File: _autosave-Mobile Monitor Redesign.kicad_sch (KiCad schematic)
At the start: 48 parts, among them J1 Conn_01x02_Pin, J2 Conn_01x08_Pin, J3 Conn_01x08_Pin, J5 Conn_02x03_Odd_Even, J6 Micro_SD_Card_Det1, J7 Conn_01x05_Pin, J8 Conn_01x06_Socket, Q1 2N7002, Q2 AO3401A, Q3 BSS138, Q4 BSS138, U1 ATmega2560-16A, U11 TPL5010, U2 DS3232M, U3 AP2112K-3.3, U4 L80-R, U7 CH340C, Y2 Crystal

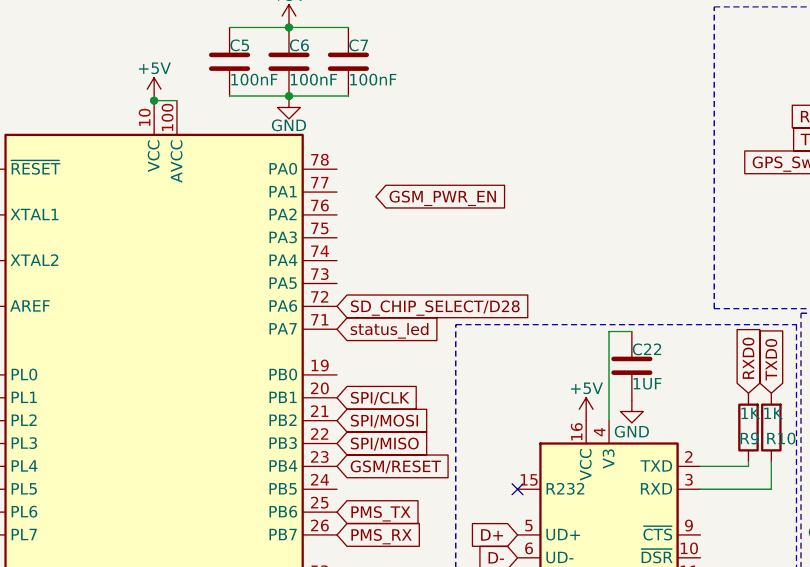
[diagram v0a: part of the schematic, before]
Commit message: added 3.3v logic level  shifting for battery monitoring chip I2C lines
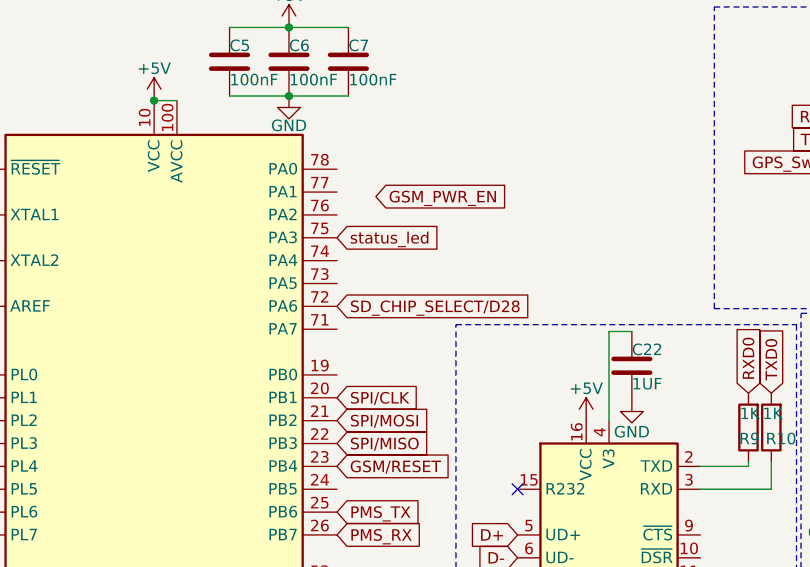
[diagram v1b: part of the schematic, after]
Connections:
- net status_led: now also U1.75 (PA3); no longer U1.71 (PA7)
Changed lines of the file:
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@@
 	(global_label "status_led"
 		(shape input)
-		(at 92.964 70.358 0)
+		(at 92.964 60.198 0)
 		(fields_autoplaced yes)
 		(effects
@@
 		)
 		(property "Intersheetrefs" "${INTERSHEET_REFS}"
-			(at 105.6252 70.358 0)
+			(at 105.6252 60.198 0)
 			(effects
 				(font
